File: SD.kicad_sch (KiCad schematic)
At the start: 2 parts, among them J4 Micro_SD_Card

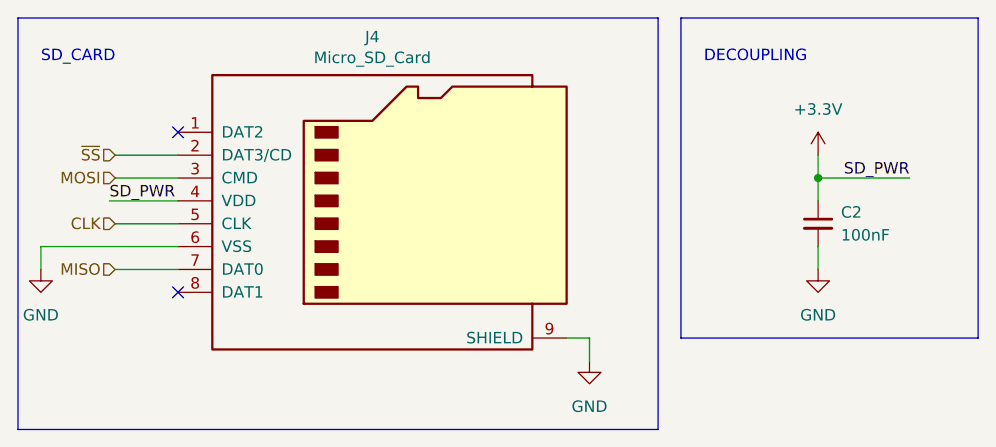
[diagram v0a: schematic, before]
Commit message: V1
- Corrected SD-cards footprint and schematical represantation;
- Corrected RTC shematics:
	- changed oscilators power supply from internal 3v3 to Vbat so RTC works when PCB is disconnected from external power supply [PWR PCB];
	- 32 kHz to microcontroller now comes from RTC module;
	- added 100 nF decoupling capacitor to Vbat RTC pin.
- Corrected couple connections and component placement on PCB
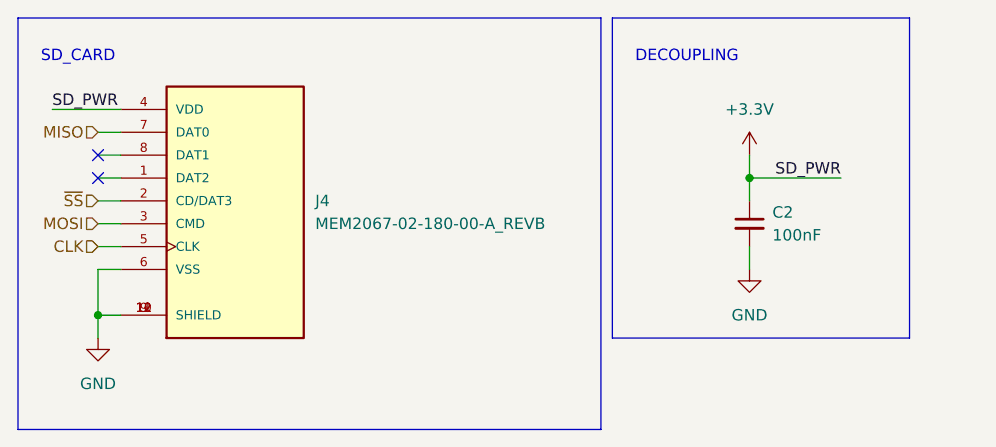
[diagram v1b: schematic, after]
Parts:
- removed J4: Micro_SD_Card, footprints:Micro_SD, symbol Connector:Micro_SD_Card
- added J4: MEM2067-02-180-00-A_REVB, footprints:GCT_MEM2067-02-180-00-A_REVB, symbol schematics:MEM2067-02-180-00-A_REVB
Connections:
- net +3V3: now also J4.4 (VDD)
- net CLK: now also J4.5 (CLK)
- net GND: now also J4.10 (SHIELD), J4.11 (SHIELD), J4.12 (SHIELD), J4.6 (VSS), J4.9 (SHIELD)
- net MISO: now also J4.7 (DAT0)
- net MOSI: now also J4.3 (CMD)
- net ~{SS}: now also J4.2 (CD/DAT3)
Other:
- company: (none) -> %%version%%
- moved on the sheet: C2
